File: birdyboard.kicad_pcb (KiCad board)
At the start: 2 copper layers, 17 parts

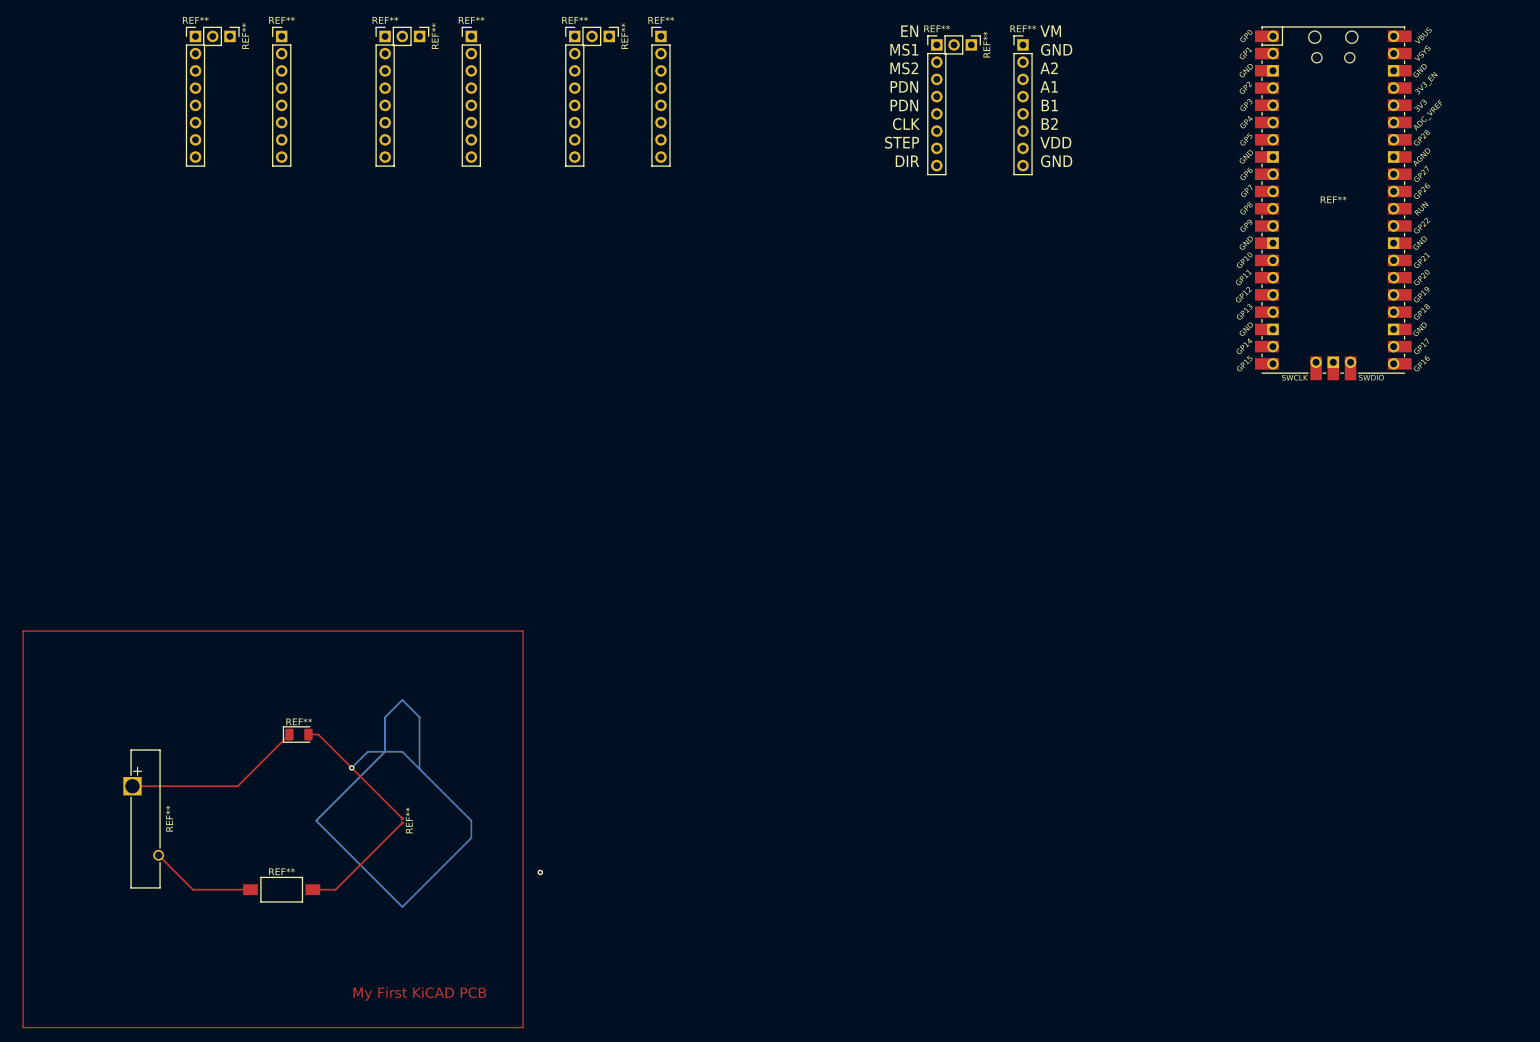
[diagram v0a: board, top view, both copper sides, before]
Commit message: Adds the main POWER terminals, adds a symbol and net names for AS5047 board header
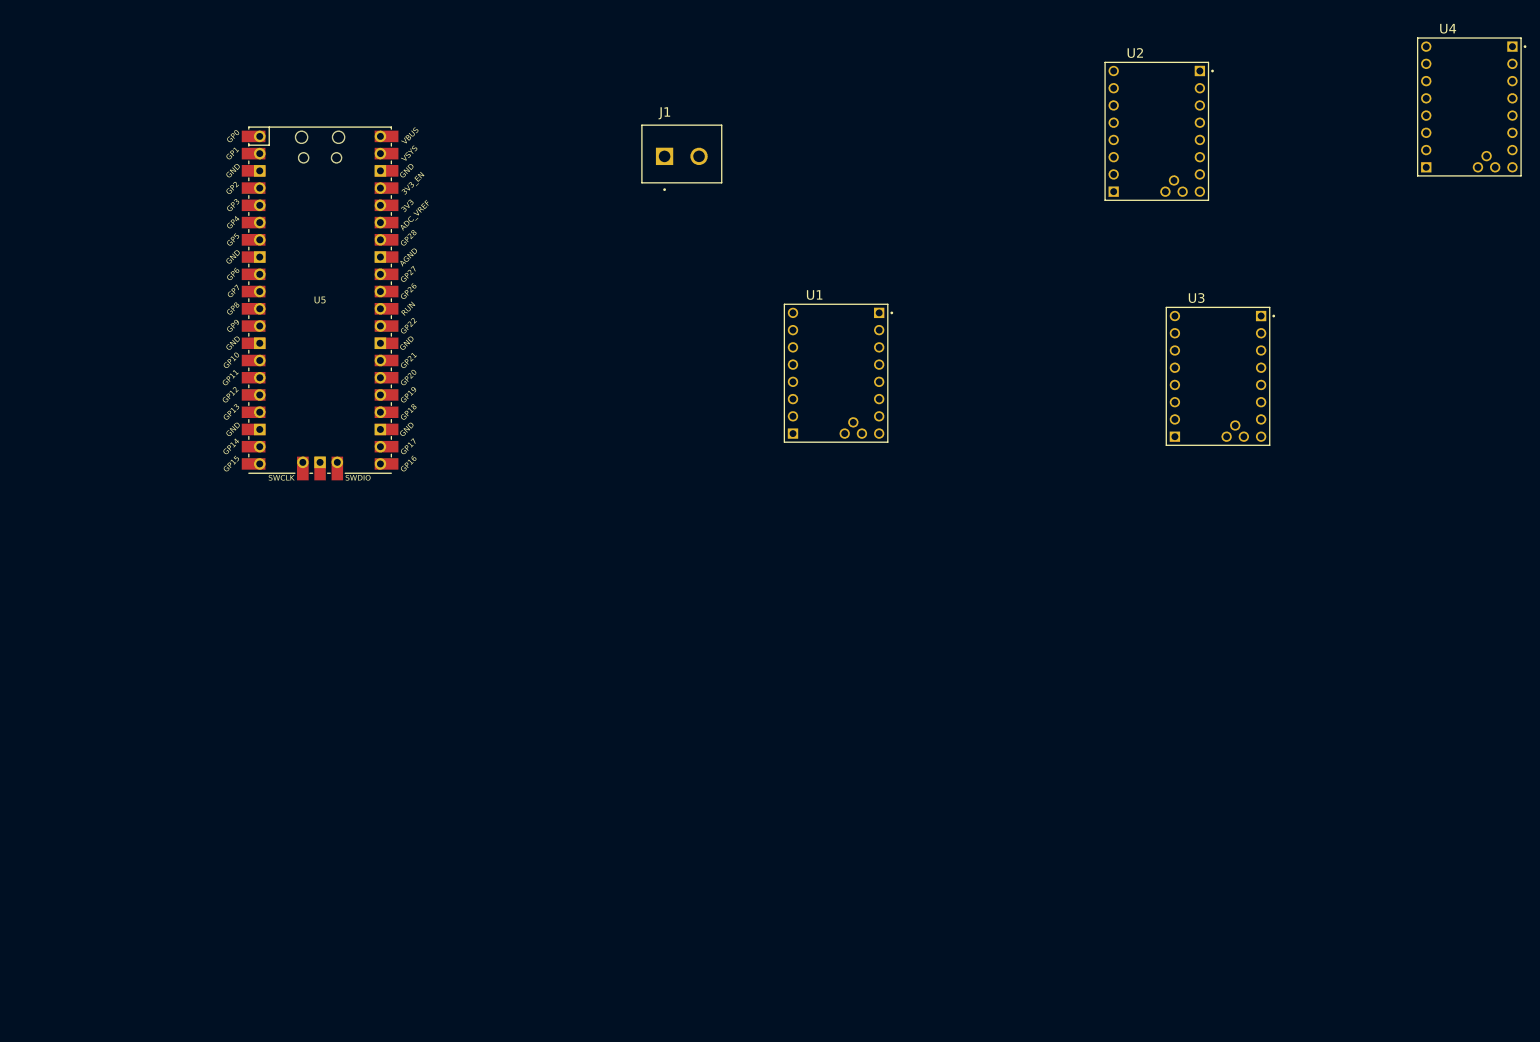
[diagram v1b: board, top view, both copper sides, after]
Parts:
- removed REF** (x8): PinHeader_1x08_P2.54mm_Vertical, Connector_PinHeader_2.54mm:PinHeader_1x08_P2.54mm_Vertical
- removed REF** (x4): PinHeader_1x02_P2.54mm_Vertical, Connector_PinHeader_2.54mm:PinHeader_1x02_P2.54mm_Vertical
- removed REF**: RPi_Pico_SMD_TH, MCU_RaspberryPi_and_Boards:RPi_Pico_SMD_TH
- removed REF**: R_0201_0603Metric, Resistor_SMD:R_0201_0603Metric
- removed REF**: SW_SPST_FSMSM, Button_Switch_SMD:SW_SPST_FSMSM
- removed REF**: D_1206_3216Metric, Diode_SMD:D_1206_3216Metric
- removed REF**: Battery_Panasonic_CR2032-VS1N_Vertical_CircularHoles, Battery:Battery_Panasonic_CR2032-VS1N_Vertical_CircularHoles
- added J1: Screw_Terminal_01x02, birdyboard:CUI_TBP01R2-508-02BE, F.Cu at (127.5, 46.9)
- added U1: TMC2208_SILENTSTEPSTICK, birdyboard:TMC2208_SILENTSTEPSTICK, F.Cu at (152.8, 78.8)
- added U2: TMC2208_SILENTSTEPSTICK, birdyboard:TMC2208_SILENTSTEPSTICK, F.Cu at (200.1, 43.2)
- added U3: TMC2208_SILENTSTEPSTICK, birdyboard:TMC2208_SILENTSTEPSTICK, F.Cu at (209.1, 79.3)
- added U4: TMC2208_SILENTSTEPSTICK, birdyboard:TMC2208_SILENTSTEPSTICK, F.Cu at (246.1, 39.6)
- added U5: Pico, MCU_RaspberryPi_and_Boards:RPi_Pico_SMD_TH, F.Cu at (76.8, 68.1)
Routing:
- net (no net): track 170.1 -> 0.00 mm, vias 2 -> 0
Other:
- board text removed: "EN MS1 MS2 PDN PDN CLK STEP DIR"
- board text removed: "My First KiCAD PCB"
- board text removed: "VM GND A2 A1 B1 B2 VDD GND"

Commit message: Adds 24-5v & 3.3v converters
-- adds 3d model for TMC2209 stepsticks
-- adds extra screw-terminal type connectors for stepper motors
-- adds a jumper to allow a single encoder to run without installing a mux
-- adds ENC_CS connections
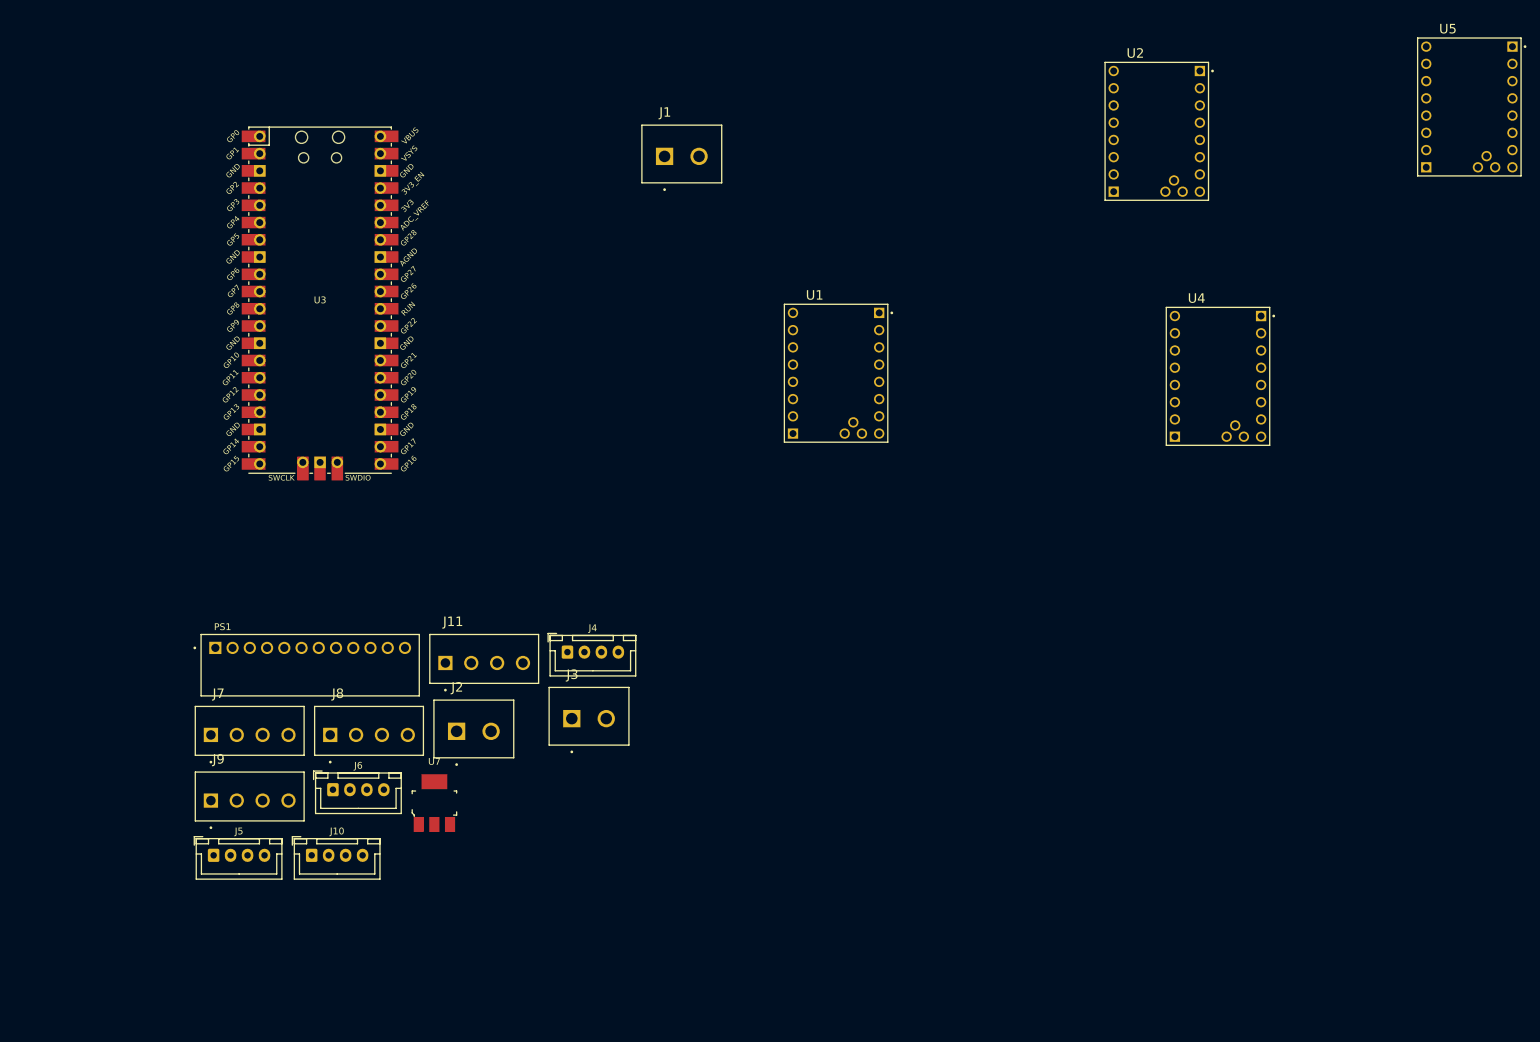
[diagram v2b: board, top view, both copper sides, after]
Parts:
- added J10: JST-PH StepMotor Conn, Connector_JST:JST_XH_B4B-XH-A_1x04_P2.50mm_Vertical, F.Cu at (75.5, 149.9)
- added J11: TBP02R2-381-04BE, birdyboard:CUI_TBP02R2-381-04BE, F.Cu at (95.2, 121.5)
- added J2: 24V Input Screw Terminal, birdyboard:CUI_TBP01R2-508-02BE, F.Cu at (96.9, 131.6)
- added J3: 24V Input Screw Terminal, birdyboard:CUI_TBP01R2-508-02BE, F.Cu at (113.9, 129.7)
- added J4: JST-PH StepMotor Conn, Connector_JST:JST_XH_B4B-XH-A_1x04_P2.50mm_Vertical, F.Cu at (113.2, 119.9)
- added J5: JST-PH StepMotor Conn, Connector_JST:JST_XH_B4B-XH-A_1x04_P2.50mm_Vertical, F.Cu at (61.1, 149.9)
- added J6: JST-PH StepMotor Conn, Connector_JST:JST_XH_B4B-XH-A_1x04_P2.50mm_Vertical, F.Cu at (78.7, 140.2)
- added J7: TBP02R2-381-04BE, birdyboard:CUI_TBP02R2-381-04BE, F.Cu at (60.7, 132.1)
- added J8: TBP02R2-381-04BE, birdyboard:CUI_TBP02R2-381-04BE, F.Cu at (78.3, 132.1)
- added J9: TBP02R2-381-04BE, birdyboard:CUI_TBP02R2-381-04BE, F.Cu at (60.7, 141.8)
- added PS1: K7805-3AR3, birdyboard:CONV_K7805-3AR3, F.Cu at (75.3, 121.9)
- added U7: AZ1117CH-3_3TRG1, digikey-footprints:SOT-223, F.Cu at (93.6, 142.2)
- J1: value Screw_Terminal_01x02 -> 24V Input Screw Terminal
- renumbered U5 to U3, U3 to U4, U4 to U5
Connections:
- J1 pad 1: unconnected-(J1-Pad1) -> (no net)
- J1 pad 2: unconnected-(J1-Pad2) -> (no net)
- U1 pad JP1_1: unconnected-(U1-PadJP1_1) -> DIR_3
- U1 pad JP1_2: unconnected-(U1-PadJP1_2) -> STEP_3
- U1 pad JP2_1: unconnected-(U1-PadJP2_1) -> +24V
- U1 pad JP2_2: Net-(U1-PadJP2_2) -> GND
- U1 pad JP2_3: unconnected-(U1-PadJP2_3) -> Net-(J4-Pad2)
- U1 pad JP2_4: unconnected-(U1-PadJP2_4) -> Net-(J4-Pad1)
- U1 pad JP2_5: unconnected-(U1-PadJP2_5) -> Net-(J4-Pad3)
- U1 pad JP2_6: unconnected-(U1-PadJP2_6) -> Net-(J4-Pad4)
- U1 pad JP2_8: Net-(U1-PadJP2_2) -> GND
- U2 pad JP1_1: unconnected-(U2-PadJP1_1) -> DIR_1
- U2 pad JP1_2: unconnected-(U2-PadJP1_2) -> STEP_1
- U2 pad JP2_1: unconnected-(U2-PadJP2_1) -> +24V
- U2 pad JP2_2: Net-(U2-PadJP2_2) -> GND
- U2 pad JP2_3: unconnected-(U2-PadJP2_3) -> Net-(J5-Pad2)
- U2 pad JP2_4: unconnected-(U2-PadJP2_4) -> Net-(J5-Pad1)
- U2 pad JP2_5: unconnected-(U2-PadJP2_5) -> Net-(J5-Pad3)
- U2 pad JP2_6: unconnected-(U2-PadJP2_6) -> Net-(J5-Pad4)
- U2 pad JP2_8: Net-(U2-PadJP2_2) -> GND
- U3 pad 10: unconnected-(U5-Pad10) -> STEP_0
- U3 pad 19: unconnected-(U5-Pad19) -> DIR_1
- U3 pad 20: unconnected-(U5-Pad20) -> STEP_1
- U3 pad 29: unconnected-(U5-Pad29) -> DIR_2
- U3 pad 34: unconnected-(U5-Pad34) -> STEP_2
- U3 pad 4: unconnected-(U5-Pad4) -> DIR_3
- U3 pad 5: unconnected-(U5-Pad5) -> STEP_3
- U3 pad 9: unconnected-(U5-Pad9) -> DIR_0
- U4 pad JP1_1: unconnected-(U3-PadJP1_1) -> DIR_0
- U4 pad JP1_2: unconnected-(U3-PadJP1_2) -> STEP_0
- U4 pad JP2_1: unconnected-(U3-PadJP2_1) -> +24V
- U4 pad JP2_2: Net-(U3-PadJP2_2) -> GND
- U4 pad JP2_3: unconnected-(U3-PadJP2_3) -> Net-(J6-Pad2)
- U4 pad JP2_4: unconnected-(U3-PadJP2_4) -> Net-(J6-Pad1)
- U4 pad JP2_5: unconnected-(U3-PadJP2_5) -> Net-(J6-Pad3)
- U4 pad JP2_6: unconnected-(U3-PadJP2_6) -> Net-(J6-Pad4)
- U4 pad JP2_8: Net-(U3-PadJP2_2) -> GND
- U5 pad JP1_1: unconnected-(U4-PadJP1_1) -> DIR_2
- U5 pad JP1_2: unconnected-(U4-PadJP1_2) -> STEP_2
- U5 pad JP2_1: unconnected-(U4-PadJP2_1) -> +24V
- U5 pad JP2_2: Net-(U4-PadJP2_2) -> GND
- U5 pad JP2_3: unconnected-(U4-PadJP2_3) -> Net-(J10-Pad2)
- U5 pad JP2_4: unconnected-(U4-PadJP2_4) -> Net-(J10-Pad1)
- U5 pad JP2_5: unconnected-(U4-PadJP2_5) -> Net-(J10-Pad3)
- U5 pad JP2_6: unconnected-(U4-PadJP2_6) -> Net-(J10-Pad4)
- U5 pad JP2_8: Net-(U4-PadJP2_2) -> GND
